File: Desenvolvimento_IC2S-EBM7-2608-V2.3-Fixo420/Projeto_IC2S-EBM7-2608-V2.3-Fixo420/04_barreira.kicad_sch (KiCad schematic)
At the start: 9 parts, among them T1 TP_+24V, T2 TP_GND_ADC_P1

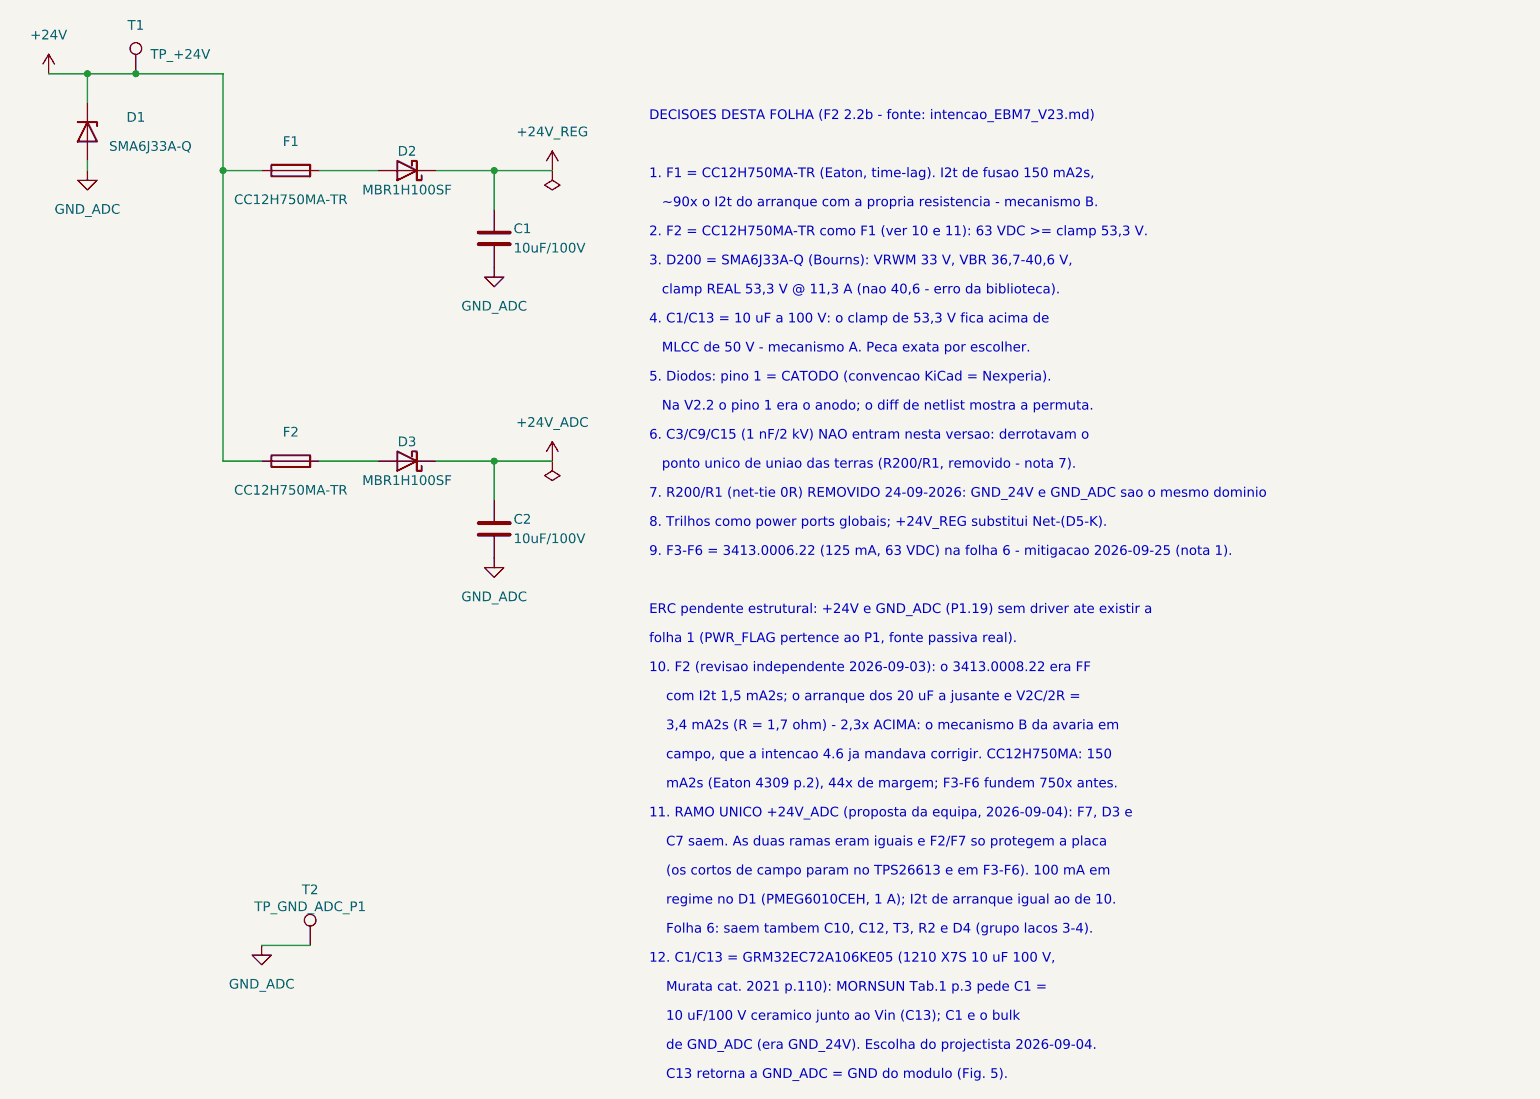
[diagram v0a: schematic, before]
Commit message: Arrumacao no padrao de pastas dos produtos (Axcel_Sensor)
Estrutura Desenvolvimento_<ID>/{Projeto_, Documentos_, Arquivos_Fabricação_}<ID>
com ID = IC2S-EBM7-2608-V2.3-Fixo420:
- Projeto: ficheiros KiCad renomeados para <ID>.kicad_*; as 322 referencias
  internas ao nome do projecto (instancias dos simbolos e .kicad_pro)
  actualizadas; bibliotecas, Outputs/drc_report.json e
  Documentos_de_Referência com os 31 datasheets das pecas desta placa.
- Documentos: 00-Especificações_Técnicas (verificacoes e relatorios),
  01-Esquemáticos (Schematic PDF, STEP, vistas topo/base), 02-Pinout e
  03-Diagrama_Blocos (vazios, como no modelo).
- Arquivos_Fabricação: Gerbers com extensoes Protel e furacao (.TXT),
  gbrjob e zip; BOM Preliminar em Excel; pick-and-place; pasta para stencil.
  Tudo gerado pelo kicad-cli e marcado PRELIMINAR (falta a revisao
  independente do roteamento).

Verificado depois da mudanca: netlist igual (148 componentes, 0 pinos com
rede diferente, nenhuma referencia perdida), ERC 0 erros, DRC 0 erros,
paridade 0, 0 por ligar. BOM: 137 pecas = soma das quantidades, 1 DNP (R8),
136 a montar; o PnP inclui ainda 8 pontos de teste e 3 fiduciais (pendente
no README).

Co-Authored-By: Claude Opus 5.5 (1M context) <noreply@anthropic.com>
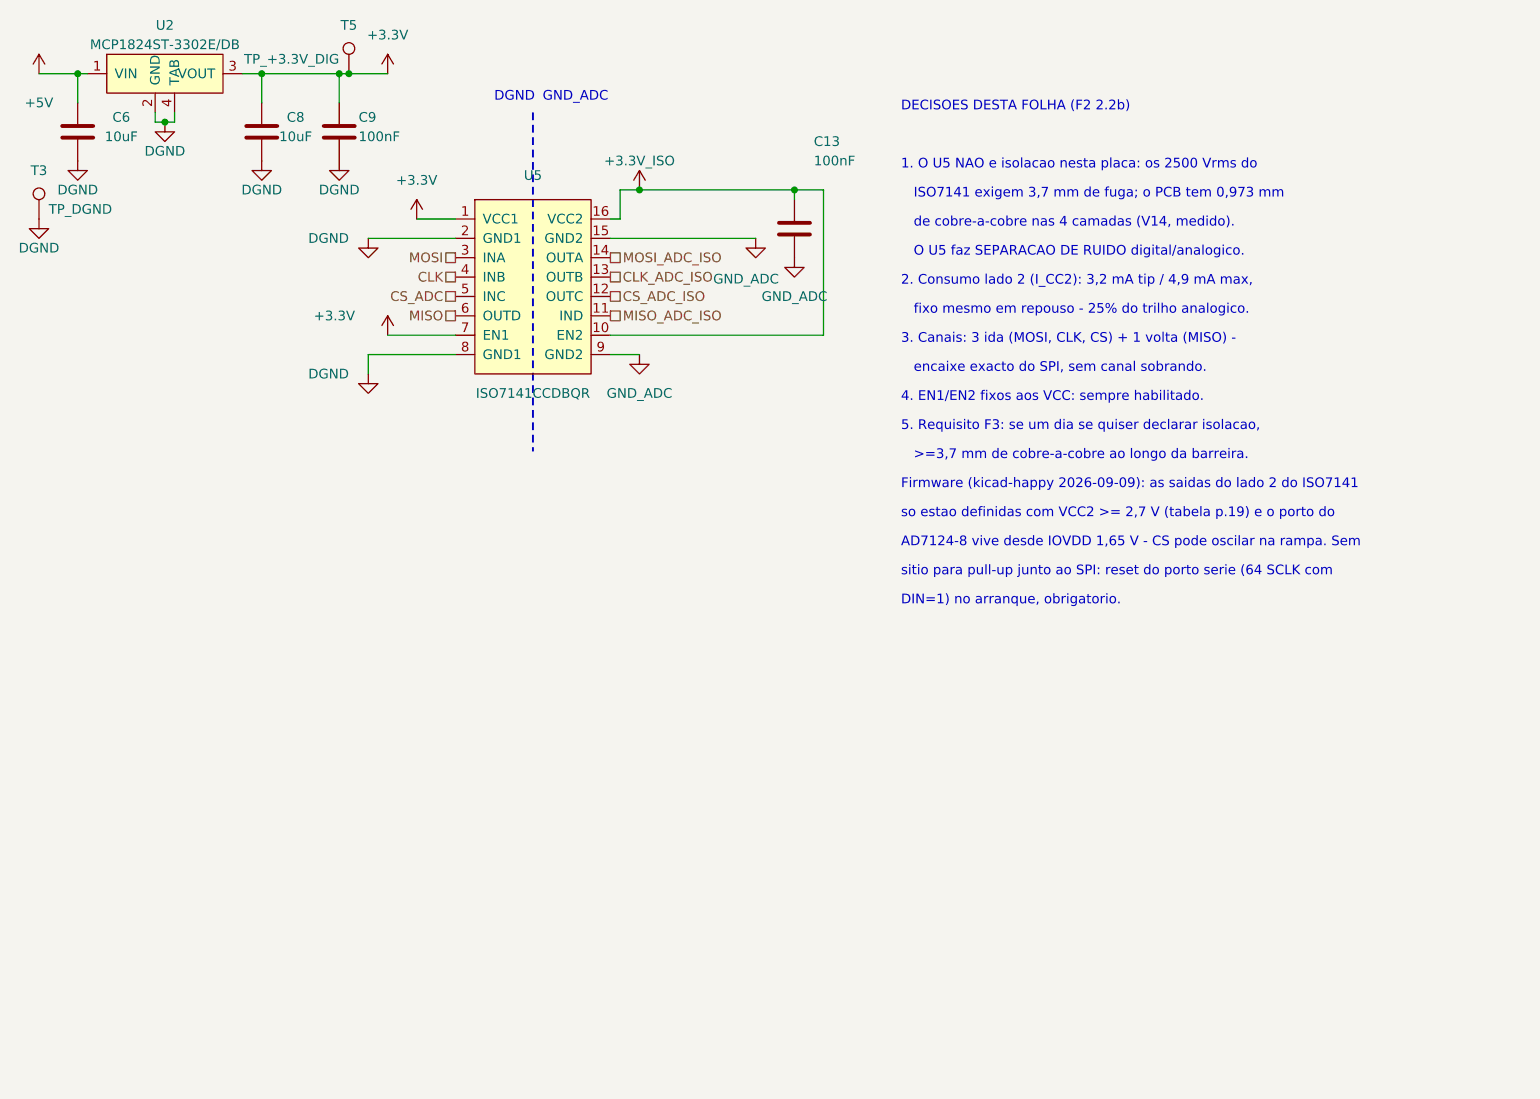
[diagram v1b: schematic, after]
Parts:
- removed C1, C2: 10uF/100V, EBM7_V23:C_1210_3225Metric, symbol Device:C
- removed D1: SMA6J33A-Q, EBM7_V23:DO-214, symbol Device:D_Zener
- removed D2, D3: MBR1H100SF, EBM7_V23:SOD123, symbol Device:D_Schottky
- removed F1, F2: CC12H750MA-TR, EBM7_V23:1206F, symbol Device:Fuse
- removed T1: TP_+24V, EBM7_V23:TestPad_Via, symbol Connector:TestPoint
- removed T2: TP_GND_ADC_P1, EBM7_V23:TestPad_Via, symbol Connector:TestPoint
- added C13, C9: 100nF, EBM7_V23:0603C, symbol Device:C
- added C6, C8: 10uF, EBM7_V23:0603C, symbol Device:C
- added T3: TP_DGND, EBM7_V23:TestPad_Via, symbol Connector:TestPoint
- added T5: TP_+3.3V_DIG, EBM7_V23:TestPad_Via, symbol Connector:TestPoint
- added U2: MCP1824ST-3302E/DB, EBM7_V23:SOT-223-3, symbol EBM7_V23_proyecto2:MCP1824ST-3302E
- added U5: ISO7141CCDBQR, EBM7_V23:SSOP16-4.9x3.9mm, symbol EBM7_V23_proyecto4:ISO7141CC
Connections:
- net GND_ADC: now also C13.2, U5.15 (GND2), U5.9 (GND2)
- new net +3.3V: C8.2, C9.1, T5.1, U2.3 (VOUT), U5.1 (VCC1), U5.7 (EN1)
- new net +3.3V_ISO: C13.1, U5.10 (EN2), U5.16 (VCC2)
- new net +5V: C6.2, U2.1 (VIN)
- new net CLK: U5.4 (INB)
- new net CLK_ADC_ISO: U5.13 (OUTB)
- new net CS_ADC: U5.5 (INC)
- new net CS_ADC_ISO: U5.12 (OUTC)
- new net DGND: C6.1, C8.1, C9.2, T3.1, U2.2 (GND), U2.4 (TAB), U5.2 (GND1), U5.8 (GND1)
- new net MISO: U5.6 (OUTD)
- new net MISO_ADC_ISO: U5.11 (IND)
- new net MOSI: U5.3 (INA)
- new net MOSI_ADC_ISO: U5.14 (OUTA)
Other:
- note added: "1. O U5 NAO e isolacao nesta placa: os 2500 Vrms do"
- note added: "2. Consumo lado 2 (I_CC2): 3,2 mA tip / 4,9 mA max,"
- note added: "3. Canais: 3 ida (MOSI, CLK, CS) + 1 volta (MISO) -"
- note added: "4. EN1/EN2 fixos aos VCC: sempre habilitado."
- note added: "5. Requisito F3: se um dia se quiser declarar isolacao,"
- note added: ">=3,7 mm de cobre-a-cobre ao longo da barreira."
- note added: "AD7124-8 vive desde IOVDD 1,65 V - CS pode oscilar na rampa. Sem"
- note added: "DECISOES DESTA FOLHA (F2 2.2b)"
- note added: "DGND"
- note added: "DIN=1) no arranque, obrigatorio."
- note added: "Firmware (kicad-happy 2026-09-09): as saidas do lado 2 do ISO7141"
- note added: "GND_ADC"
- note added: "ISO7141 exigem 3,7 mm de fuga; o PCB tem 0,973 mm"
- note added: "O U5 faz SEPARACAO DE RUIDO digital/analogico."
- note added: "de cobre-a-cobre nas 4 camadas (V14, medido)."
- note added: "encaixe exacto do SPI, sem canal sobrando."
- note added: "fixo mesmo em repouso - 25% do trilho analogico."
- note added: "sitio para pull-up junto ao SPI: reset do porto serie (64 SCLK com"
- note added: "so estao definidas com VCC2 >= 2,7 V (tabela p.19) e o porto do"
- note removed: "(os cortos de campo param no TPS26613 e em F3-F6). 100 mA em"
- note removed: "1. F1 = CC12H750MA-TR (Eaton, time-lag). I2t de fusao 150 mA2s,"
- note removed: "10 uF/100 V ceramico junto ao Vin (C13); C1 e o bulk"
- note removed: "10. F2 (revisao independente 2026-09-03): o 3413.0008.22 era FF"
- note removed: "11. RAMO UNICO +24V_ADC (proposta da equipa, 2026-09-04): F7, D3 e"
- note removed: "12. C1/C13 = GRM32EC72A106KE05 (1210 X7S 10 uF 100 V,"
- note removed: "2. F2 = CC12H750MA-TR como F1 (ver 10 e 11): 63 VDC >= clamp 53,3 V."
- note removed: "3,4 mA2s (R = 1,7 ohm) - 2,3x ACIMA: o mecanismo B da avaria em"
- note removed: "3. D200 = SMA6J33A-Q (Bourns): VRWM 33 V, VBR 36,7-40,6 V,"
- note removed: "4. C1/C13 = 10 uF a 100 V: o clamp de 53,3 V fica acima de"
- note removed: "5. Diodos: pino 1 = CATODO (convencao KiCad = Nexperia)."
- note removed: "6. C3/C9/C15 (1 nF/2 kV) NAO entram nesta versao: derrotavam o"
- note removed: "7. R200/R1 (net-tie 0R) REMOVIDO 24-09-2026: GND_24V e GND_ADC sao o mesmo dominio"
- note removed: "8. Trilhos como power ports globais; +24V_REG substitui Net-(D5-K)."
- note removed: "9. F3-F6 = 3413.0006.22 (125 mA, 63 VDC) na folha 6 - mitigacao 2026-09-25 (nota 1)."
- note removed: "C13 retorna a GND_ADC = GND do modulo (Fig. 5)."
- note removed: "C7 saem. As duas ramas eram iguais e F2/F7 so protegem a placa"
- note removed: "DECISOES DESTA FOLHA (F2 2.2b - fonte: intencao_EBM7_V23.md)"
- note removed: "ERC pendente estrutural: +24V e GND_ADC (P1.19) sem driver ate existir a"
- note removed: "Folha 6: saem tambem C10, C12, T3, R2 e D4 (grupo lacos 3-4)."
- note removed: "MLCC de 50 V - mecanismo A. Peca exata por escolher."
- note removed: "Murata cat. 2021 p.110): MORNSUN Tab.1 p.3 pede C1 ="
- note removed: "Na V2.2 o pino 1 era o anodo; o diff de netlist mostra a permuta."
- note removed: "campo, que a intencao 4.6 ja mandava corrigir. CC12H750MA: 150"
- note removed: "clamp REAL 53,3 V @ 11,3 A (nao 40,6 - erro da biblioteca)."
- note removed: "com I2t 1,5 mA2s; o arranque dos 20 uF a jusante e V2C/2R ="
- note removed: "de GND_ADC (era GND_24V). Escolha do projectista 2026-09-04."
- note removed: "folha 1 (PWR_FLAG pertence ao P1, fonte passiva real)."
- note removed: "mA2s (Eaton 4309 p.2), 44x de margem; F3-F6 fundem 750x antes."
- note removed: "ponto unico de uniao das terras (R200/R1, removido - nota 7)."
- note removed: "regime no D1 (PMEG6010CEH, 1 A); I2t de arranque igual ao de 10."
- note removed: "~90x o I2t do arranque com a propria resistencia - mecanismo B."

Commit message: Revisao da reuniao 28-09: ramo unico de 24 V, 100 nF a 50 V, um so MPN de 1 uF
- Saem F2, o diodo e o condensador do ramo +24V_ADC; F1 + diodo alimentam o
  R-78HB e o +24V_ADC. +24V_REG deixa de existir (esquematico, PCB, netclasses).
- Condensador de entrada do R-78HB conferido contra o datasheet Recom (p.4):
  10 uF/100 V cumpre os 3,3 uF/100 V pedidos com Vin > 50 V. Sem alteracao.
- 100 nF fora do 24 V -> TDK C1608X7R1H104K080AA (50 V); o do +24V_ADC fica
  GRM188R72A104KA35D (100 V). 1 uF -> TDK C1608X7R1H105K080AB nos quatro.
- Notas 2, 13 e 14 da folha 2; README e registo em 00-Especificacoes;
  catalogo TDK em Documentos_de_Referencia.

Co-Authored-By: Claude Opus 5.5 (1M context) <noreply@anthropic.com>
Claude-Session: https://claude.ai/code/session_01KPnkiJQKrkjgRqqw9M78ie
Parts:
- C13, C9: value 100nF -> 100nF/50V; MPN GRM188R72A104KA35D -> C1608X7R1H104K080AA
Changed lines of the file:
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@@
 			)
 		)
-		(property "Value" "100nF"
+		(property "Value" "100nF/50V"
 			(at 76.2 59.055 0)
 			(show_name no)
@@
 			)
 		)
-		(property "MPN" "GRM188R72A104KA35D"
+		(property "MPN" "C1608X7R1H104K080AA"
 			(at -50.8 -88.9 0)
 			(hide yes)
@@
 			)
 		)
-		(property "Value" "100nF"
+		(property "Value" "100nF/50V"
 			(at 135.89 62.23 0)
 			(show_name no)
@@
 			)
 		)
-		(property "MPN" "GRM188R72A104KA35D"
+		(property "MPN" "C1608X7R1H104K080AA"
 			(at 6.35 0 0)
 			(hide yes)

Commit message: LDO 3,3 V do lado PLC: U2 MCP1824ST (SOT-223) -> SPX3819M5-L-3-3/TR (SOT-23-5), mesmo MPN do U3
- Criterio da equipa: menos MPN, mais pecas do mesmo tipo; o MCP1824ST sai.
- EN a VIN, BYP aberto; estabilidade com ceramico sem garantia no datasheet (provada em campo na V2.2).
- Esquematico: ERC 0; netlist so muda os pinos do U2. PCB: pegada SOT-23-5 no
  mesmo sitio; faltam rotear 6 ligacoes do U2; Gerbers/PnP por regenerar depois.
- Registo: alteracao_LDO_3V3_lado_PLC_2026-09-28.md (comparacao, verificacao e
  riscos em aberto). BOM e PDF do esquematico regenerados.

Co-Authored-By: Claude Opus 5.5 (1M context) <noreply@anthropic.com>
Claude-Session: https://claude.ai/code/session_01KPnkiJQKrkjgRqqw9M78ie
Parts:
- U2: value MCP1824ST-3302E/DB -> SPX3819M5-L-3-3/TR; footprint EBM7_V23:SOT-223-3 -> EBM7_V23:SOT-23-5; symbol EBM7_V23_proyecto2:MCP1824ST-3302E -> Regulator_Linear:SPX3819M5-L-3-3; MPN MCP1824ST-3302E/DB -> SPX3819M5-L-3-3/TR
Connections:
- net +3.3V: now also U2.5 (OUT); no longer U2.3 (VOUT)
- net +5V: now also U2.3 (EN)
- net DGND: no longer U2.4 (TAB)
- no-connect marks 0 -> 1
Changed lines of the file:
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@@
-	)
-	(junction
-		(at 50.8 57.15)
-		(diameter 0)
-		(color 0 0 0 0)
 	)
 	(junction
@@
 	(wire
 		(pts
-			(xy 49.53 55.88) (xy 49.53 57.15)
-		)
-		(stroke
-			(width 0)
-			(type default)
-		)
-	)
-	(wire
-		(pts
 			(xy 133.35 66.04) (xy 133.35 67.31)
-		)
-		(stroke
-			(width 0)
-			(type default)
-		)
-	)
-	(wire
-		(pts
-			(xy 50.8 57.15) (xy 52.07 57.15)
 		)
 		(stroke
@@
 	(wire
 		(pts
-			(xy 52.07 57.15) (xy 52.07 55.88)
-		)
-		(stroke
-			(width 0)
-			(type default)
-		)
-	)
-	(wire
-		(pts
 			(xy 73.66 50.8) (xy 73.66 54.61)
 		)
@@
 		(pts
 			(xy 39.37 50.8) (xy 40.64 50.8)
-		)
-		(stroke
-			(width 0)
-			(type default)
-		)
-	)
-	(wire
-		(pts
-			(xy 49.53 57.15) (xy 50.8 57.15)
 		)
 		(stroke
@@
 	(symbol
 		(lib_id "power:GND")
-		(at 50.8 57.15 0)
+		(at 50.8 60.96 0)
 		(unit 1)
 		(body_style 1)
@@
 		(dnp no)
 		(property "Reference" "#PWR030"
-			(at 50.8 50.8 0)
+			(at 50.8 54.61 0)
 			(hide yes)
 			(show_name no)
@@
 		)
 		(property "Value" "DGND"
+			(at 50.8 64.77 0)
+			(show_name no)
+			(do_not_autoplace no)
+			(effects
+				(font
+					(size 1.27 1.27)
+				)
+			)
+		)
+		(property "Footprint" ""
 			(at 50.8 60.96 0)
-			(show_name no)
-			(do_not_autoplace no)
-			(effects
-				(font
-					(size 1.27 1.27)
-				)
-			)
-		)
-		(property "Footprint" ""
-			(at 50.8 57.15 0)
-			(hide yes)
-			(show_name no)
-			(do_not_autoplace no)
-			(effects
-				(font
-					(size 1.27 1.27)
-				)
-			)
-		)
-		(property "Datasheet" ""
-			(at 50.8 57.15 0)
-			(hide yes)
-			(show_name no)
-			(do_not_autoplace no)
-			(effects
-				(font
-					(size 1.27 1.27)
-				)
-			)
-		)
-		(property "Description" ""
-			(at 50.8 57.15 0)
+			(hide yes)
+			(show_name no)
+			(do_not_autoplace no)
+			(effects
+				(font
+					(size 1.27 1.27)
+				)
+			)
+		)
+		(property "Datasheet" ""
+			(at 50.8 60.96 0)
+			(hide yes)
+			(show_name no)
+			(do_not_autoplace no)
+			(effects
+				(font
+					(size 1.27 1.27)
+				)
+			)
+		)
+		(property "Description" ""
+			(at 50.8 60.96 0)
 			(show_name no)
 			(do_not_autoplace no)
@@
 	)
 	(symbol
-		(lib_id "EBM7_V23_proyecto2:MCP1824ST-3302E")
-		(at 50.8 50.8 0)
+		(lib_id "Regulator_Linear:SPX3819M5-L-3-3")
+		(at 50.8 53.34 0)
 		(unit 1)
 		(body_style 1)
@@
 			)
 		)
-		(property "Value" "MCP1824ST-3302E/DB"
+		(property "Value" "SPX3819M5-L-3-3/TR"
 			(at 50.8 46.99 0)
 			(show_name no)
@@
 			)
 		)
-		(property "Footprint" "EBM7_V23:SOT-223-3"
+		(property "Footprint" "EBM7_V23:SOT-23-5"
 			(at 50.8 50.8 0)
 			(hide yes)
@@
 			)
 		)
-		(property "MPN" "MCP1824ST-3302E/DB"
+		(property "MPN" "SPX3819M5-L-3-3/TR"
 			(at -50.8 -88.9 0)
 			(hide yes)
@@
 		(pin "1"
 		)
+		(pin "2"
+		)
 		(pin "3"
 		)
 		(pin "4"
 		)
-		(pin "2"
+		(pin "5"
 		)
 		(instances
@@
 		)
 	)
+	(wire
+		(pts
+			(xy 40.64 50.8) (xy 41.91 50.8)
+		)
+		(stroke
+			(width 0)
+			(type default)
+		)
+	)
+	(wire
+		(pts
+			(xy 41.91 50.8) (xy 43.18 50.8)
+		)
+		(stroke
+			(width 0)
+			(type default)
+		)
+	)
+	(wire
+		(pts
+			(xy 43.18 53.34) (xy 41.91 53.34)
+		)
+		(stroke
+			(width 0)
+			(type default)
+		)
+	)
+	(wire
+		(pts
+			(xy 41.91 53.34) (xy 41.91 50.8)
+		)
+		(stroke
+			(width 0)
+			(type default)
+		)
+	)
+	(wire
+		(pts
+			(xy 58.42 50.8) (xy 60.96 50.8)
+		)
+		(stroke
+			(width 0)
+			(type default)
+		)
+	)
+	(junction
+		(at 41.91 50.8)
+		(diameter 0)
+		(color 0 0 0 0)
+	)
+	(no_connect
+		(at 58.42 53.34)
+	)
 	(sheet_instances
